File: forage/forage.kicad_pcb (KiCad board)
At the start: 2 copper layers, 312.7 x 79.4 mm, 70 parts, among them J1 Conn_01x04_MountingPin, Q1 AO3400A, U1 STM32G431RBTx, U2 XC6206P332MR

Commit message: reestablish connections, todo: smooth tracks
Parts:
- moved C1 4.62 mm to (323.1, 150.2)
- moved C13 4.62 mm to (321.5, 154.5)
- moved C2 4.62 mm to (326.4, 150.2)
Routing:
- net PRTSC: track 0.00 -> 65.0 mm
- net RIGHT: track 0.00 -> 57.8 mm
- net DELETE: track 0.00 -> 56.1 mm
- net DOWN: track 0.00 -> 38.9 mm
- net GND: track 1224.3 -> 1261.8 mm
- net INSERT: track 0.00 -> 35.8 mm
- net UP: track 0.00 -> 23.5 mm
- net LEFT: track 0.87 -> 22.3 mm
- net Net-(U1-VREF+): track 11.3 -> 15.8 mm
- net +3.3V: track 91.9 -> 94.8 mm

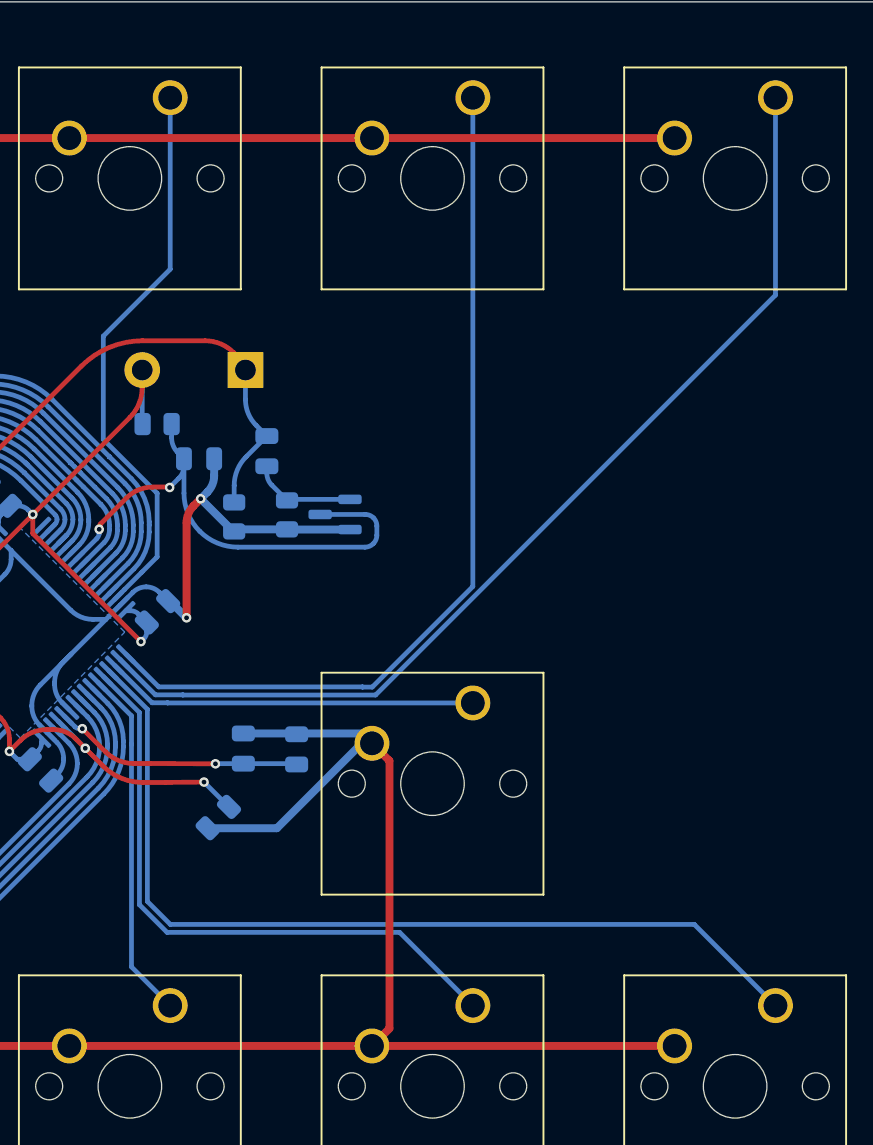
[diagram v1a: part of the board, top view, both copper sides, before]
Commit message: smooth the new tracks
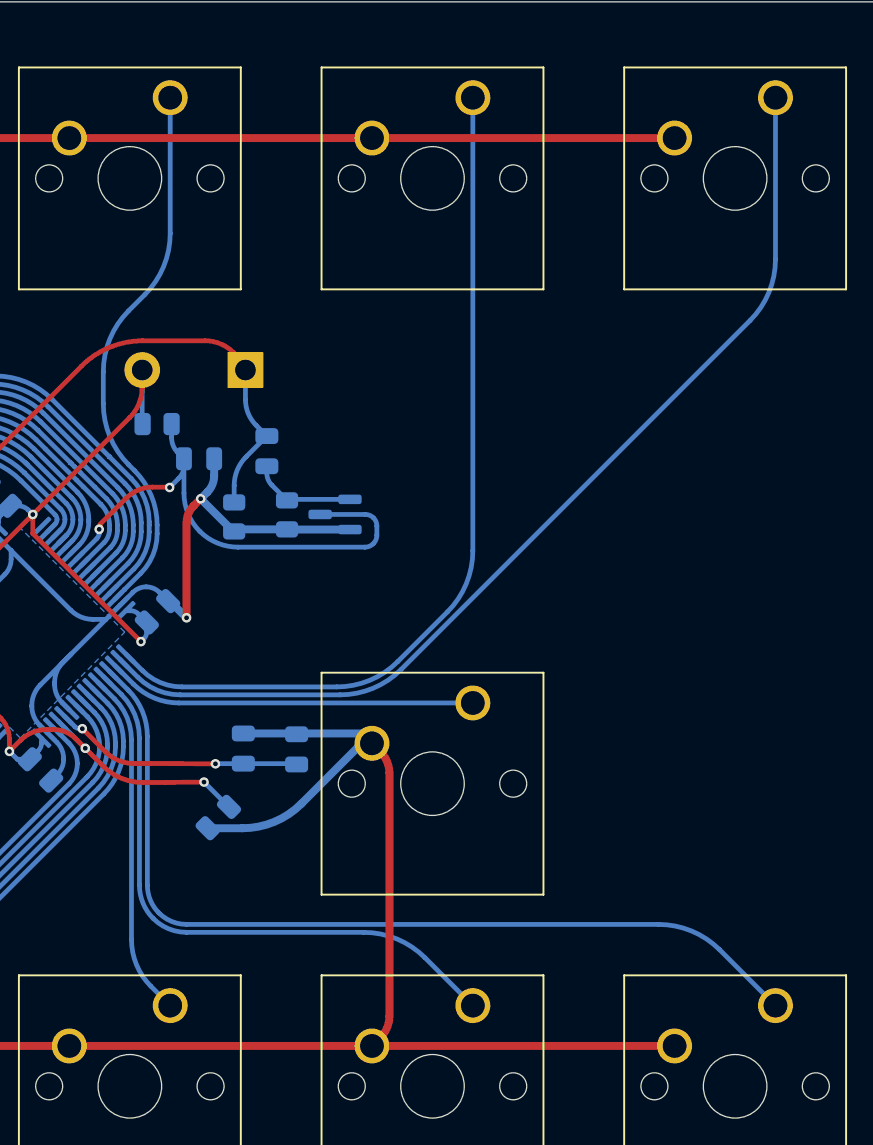
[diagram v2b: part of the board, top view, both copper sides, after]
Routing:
- net INSERT: track 35.8 -> 34.7 mm
- net DOWN: track 38.9 -> 38.2 mm
- net PRTSC: track 65.0 -> 64.3 mm
- net DELETE: track 56.1 -> 55.4 mm
- net RIGHT: track 57.8 -> 57.1 mm
